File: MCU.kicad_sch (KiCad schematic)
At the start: 112 parts, among them J1 Conn_01x02_Pin, J11 Logger Connector, J12 UART Connector, J13 External UART, J14 External I2C, J15 JTAG Header, J2 Conn_01x02_Pin, J27 Conn_01x02_Pin, SW1 XRSn_button, U13 M24M01E-FMN6TP, U17 TRS3221EIPWR, U18 BZX84C3V3TS-7-F, U19 BZX84C3V3TS-7-F, U20 BZX84C3V3TS-7-F, U21 MIC920YC5-TR, U5 F280025PNS, Y2 H130B-16.000-18-3030-EXT-TR

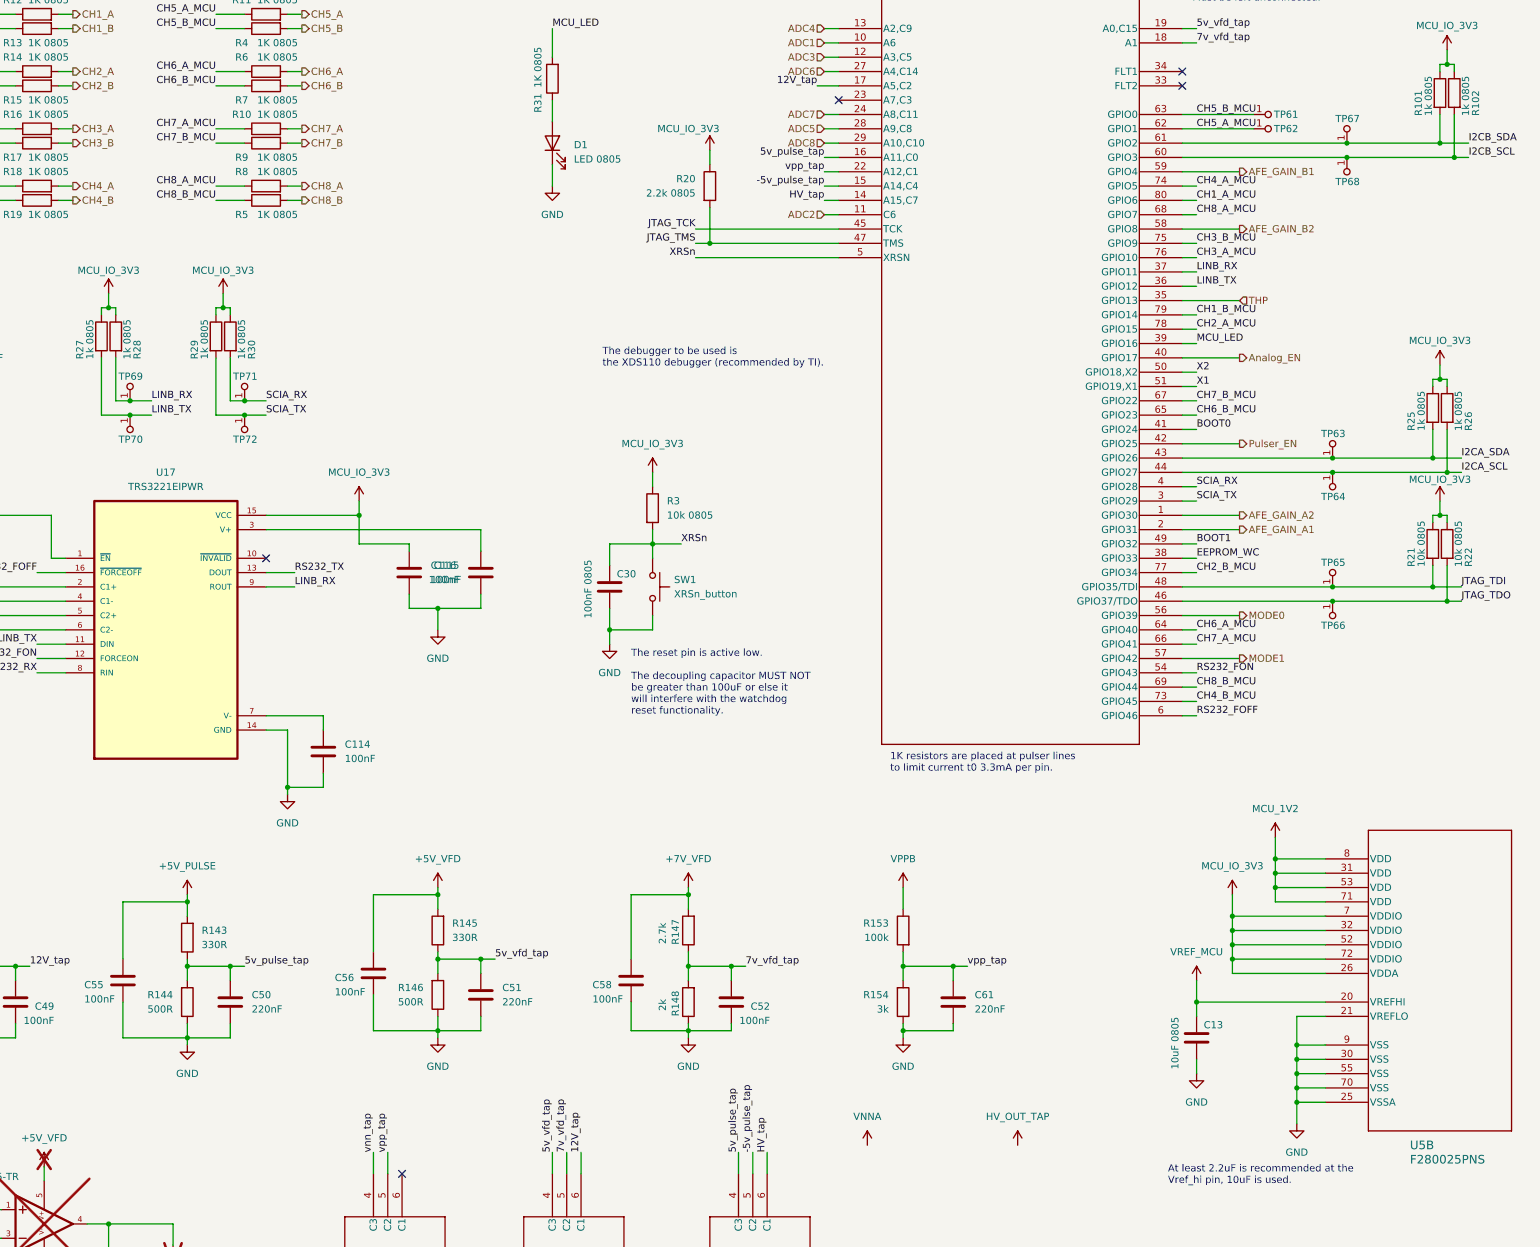
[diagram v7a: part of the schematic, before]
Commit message: added test points & fuse
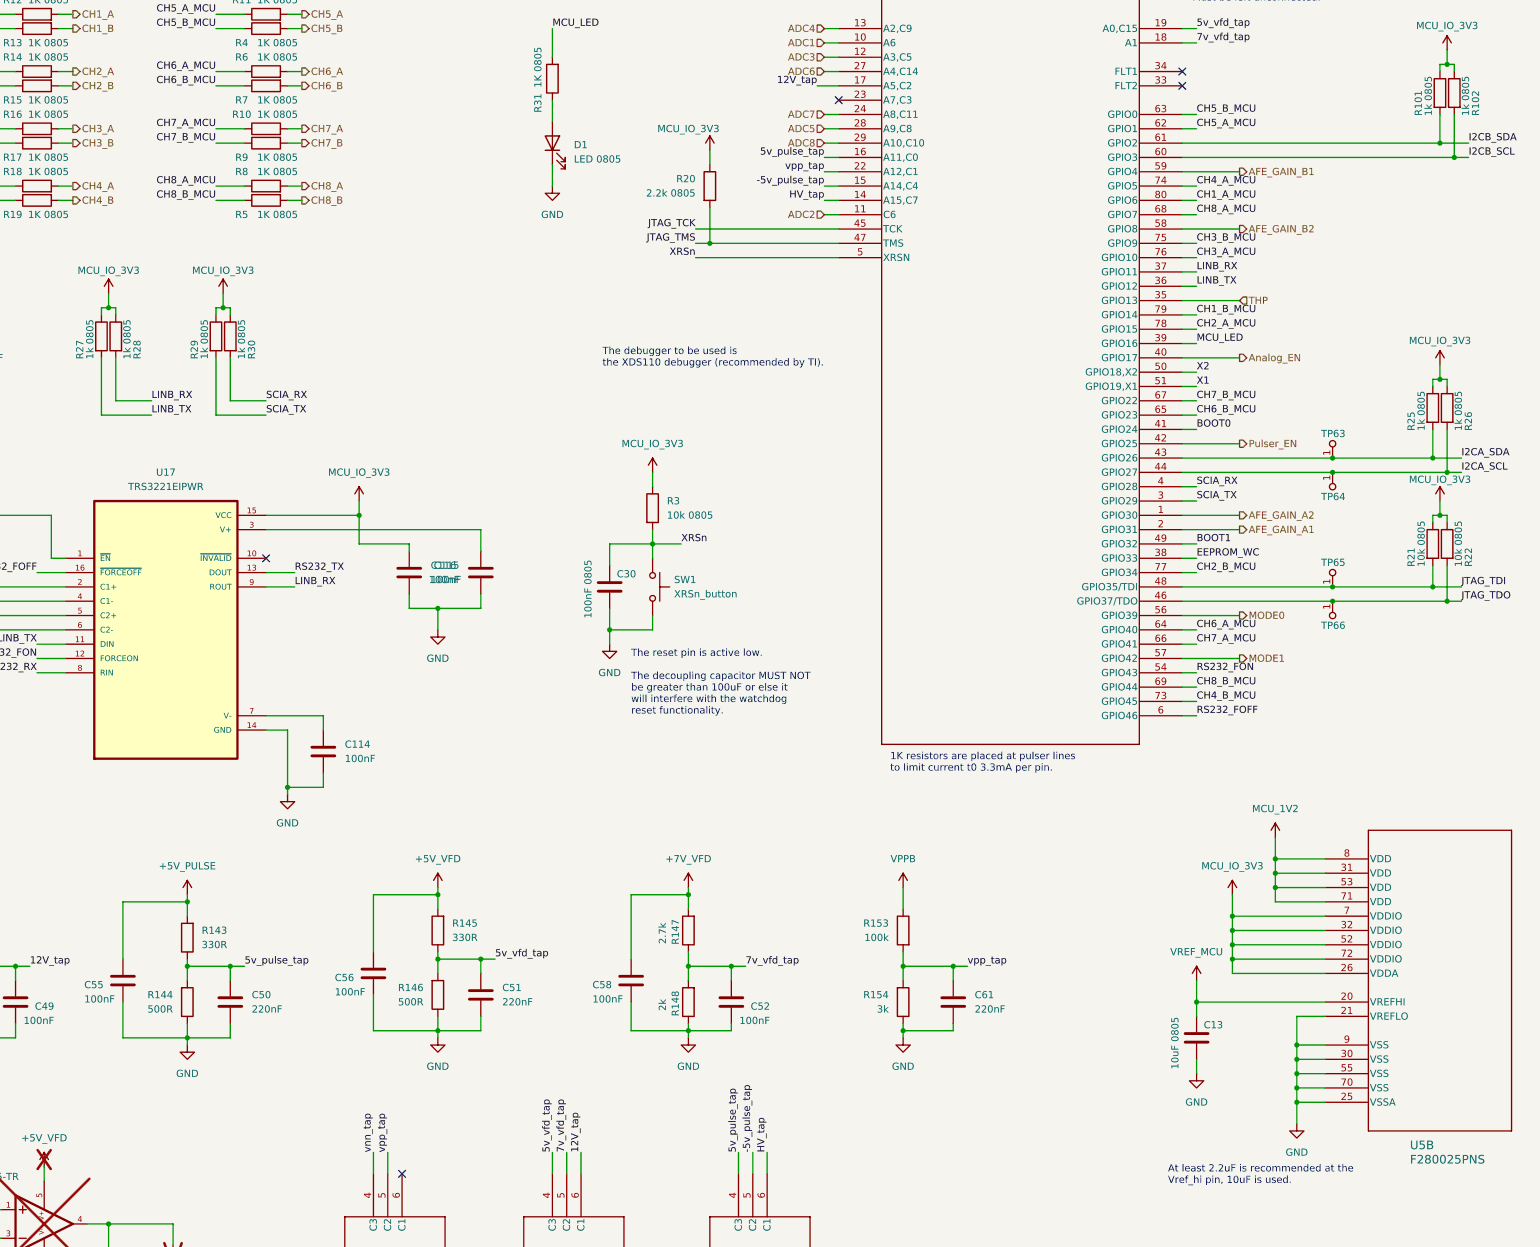
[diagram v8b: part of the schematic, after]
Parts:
- removed TP61, TP62, TP67, TP68, TP69, TP70, TP71, TP72: RCT-0C, digikey-footprints:PROBE_PAD_0805, symbol dk_Test-Points:RCT-0C
